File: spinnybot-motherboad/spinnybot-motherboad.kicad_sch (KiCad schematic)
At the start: 48 parts, among them J1 +12V, J11 CAP SWITCH, J12 LEDSTRIP3, J13 LEDSTRIP2, J14 LEDSTRIP3, J2 LEDSTRIP1, J3 LEDSTRIP1, J4 LEDSTRIP2, J5 GND, J6 MOTOR2, J7 MOTOR3, J8 MOTOR1, J9 CAP SWITCH, Q1 SISA96DN, Q2 SISA96DN, Q4 2N3904, Q5 2N3906, U1 LM1117-3.3, U2 XBP9B-DMWT-002, U3 SN74LVC1G74

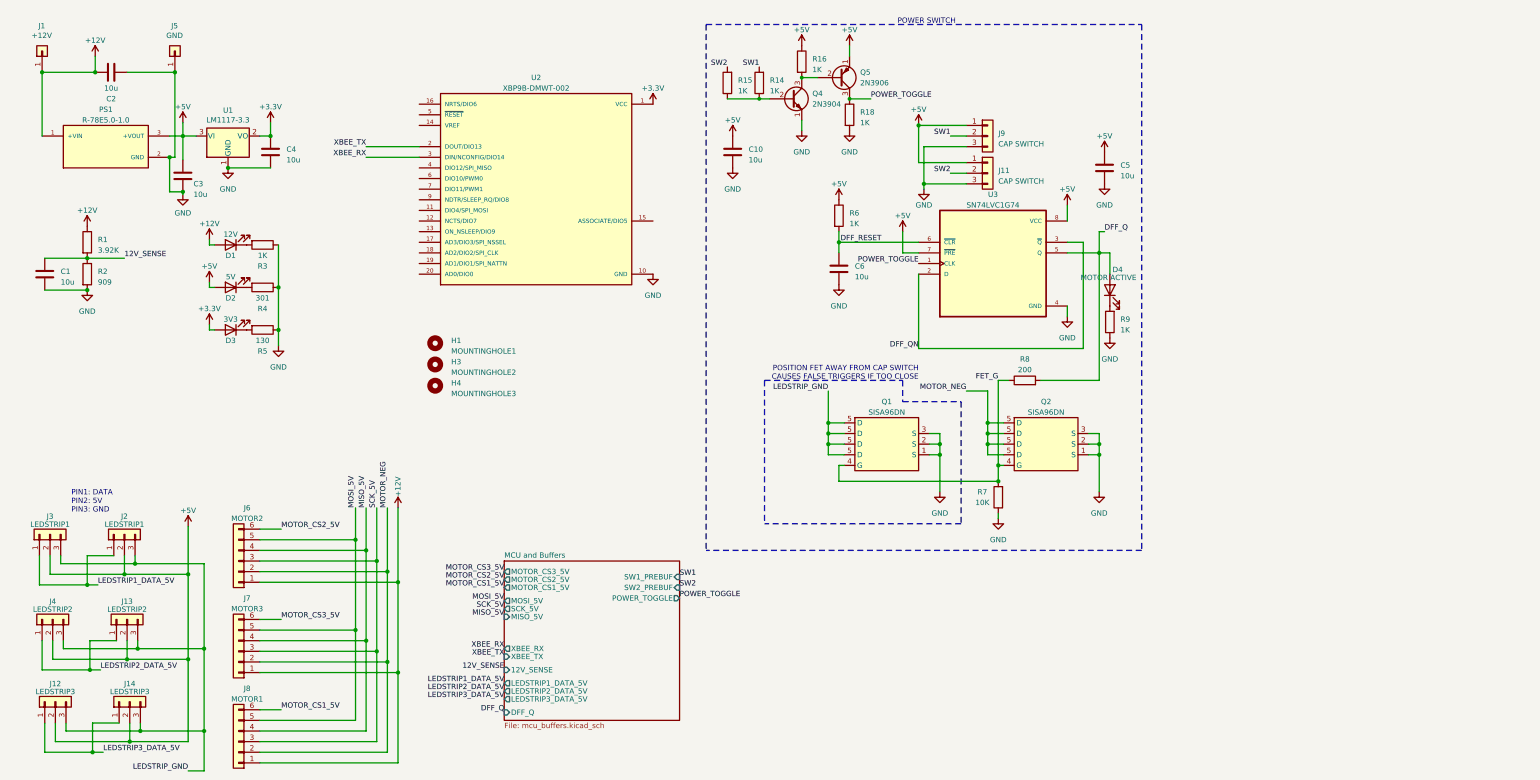
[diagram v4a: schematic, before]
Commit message: split schematic into multiple files and stole Erick's homework on redoing the power button
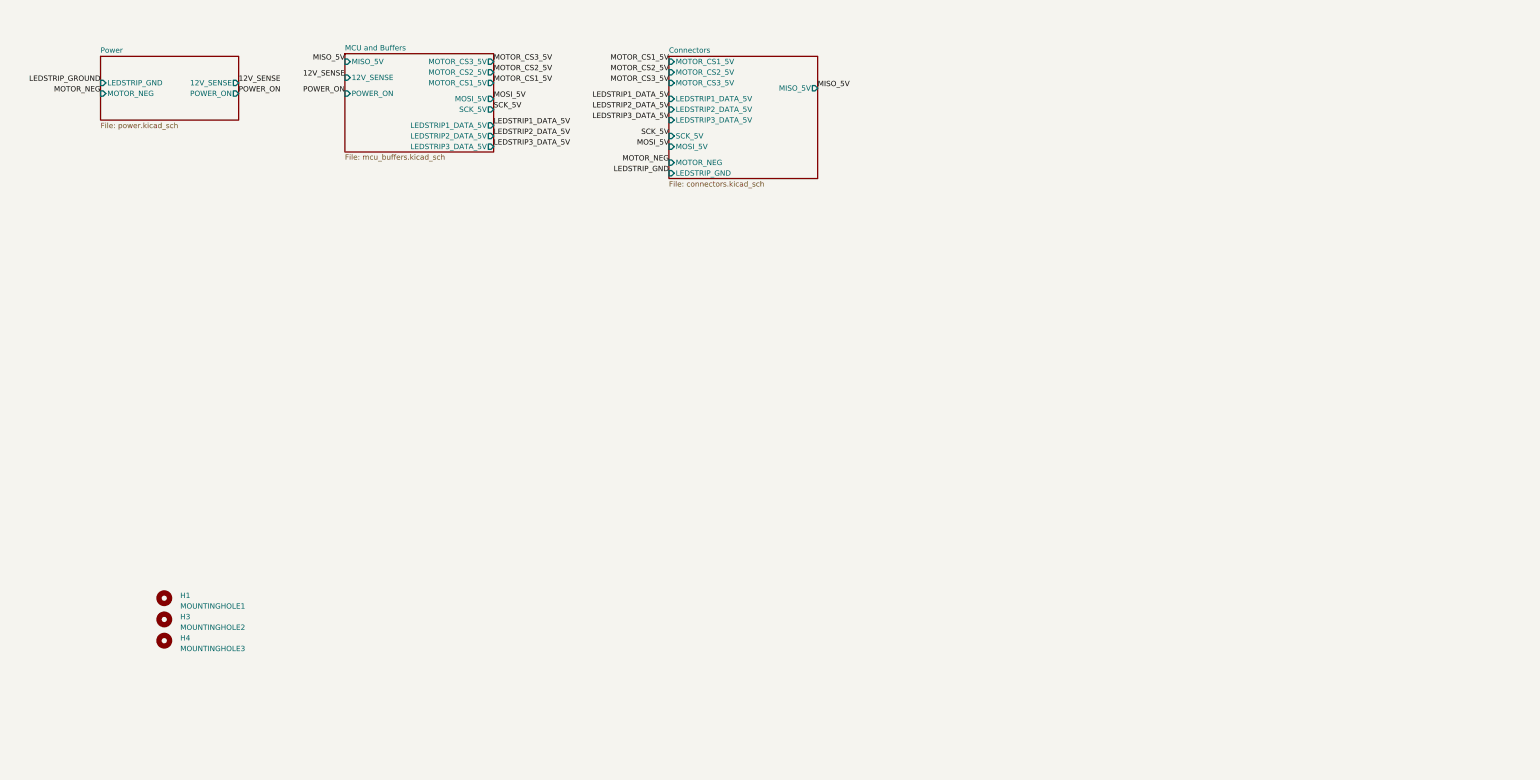
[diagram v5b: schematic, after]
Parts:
- removed C1, C10, C3, C4, C5, C6: 10u, Capacitor_SMD:C_1206_3216Metric_Pad1.33x1.80mm_HandSolder, symbol Device:C
- removed C2: 10u, Capacitor_SMD:C_0805_2012Metric_Pad1.18x1.45mm_HandSolder, symbol Device:C
- removed D1: 12V, LED_SMD:LED_0805_2012Metric_Pad1.15x1.40mm_HandSolder, symbol Device:LED
- removed D2: 5V, LED_SMD:LED_0805_2012Metric_Pad1.15x1.40mm_HandSolder, symbol Device:LED
- removed D3: 3V3, LED_SMD:LED_0805_2012Metric_Pad1.15x1.40mm_HandSolder, symbol Device:LED
- removed D4: MOTOR ACTIVE, LED_SMD:LED_0805_2012Metric_Pad1.15x1.40mm_HandSolder, symbol Device:LED
- removed J1: +12V, Connector_Wire:SolderWirePad_1x01_SMD_5x10mm, symbol Connector_Generic:Conn_01x01
- removed J11, J9: CAP SWITCH, B3B-PH-SM4:JST_B3B-PH-SM4-TB(LF)(SN), symbol Connector_Generic:Conn_01x03
- removed J12, J14: LEDSTRIP3, B3B-PH-SM4:JST_B3B-PH-SM4-TB(LF)(SN), symbol Connector_Generic:Conn_01x03
- removed J13, J4: LEDSTRIP2, B3B-PH-SM4:JST_B3B-PH-SM4-TB(LF)(SN), symbol Connector_Generic:Conn_01x03
- removed J2, J3: LEDSTRIP1, B3B-PH-SM4:JST_B3B-PH-SM4-TB(LF)(SN), symbol Connector_Generic:Conn_01x03
- removed J5: GND, custom:Stitched_SolderWirePad_1x01_SMD_5x10mm, symbol Connector_Generic:Conn_01x01
- removed J6: MOTOR2, S6B-XH-SM4-TB:S6B-XH-SM4-TBLFSN, symbol Connector_Generic:Conn_01x06
- removed J7: MOTOR3, S6B-XH-SM4-TB:S6B-XH-SM4-TBLFSN, symbol Connector_Generic:Conn_01x06
- removed J8: MOTOR1, S6B-XH-SM4-TB:S6B-XH-SM4-TBLFSN, symbol Connector_Generic:Conn_01x06
- removed PS1: R-78E5.0-1.0, R-78E5:CONV_R-78E5.0-1.0, symbol R-78E5.0-1.0:R-78E5.0-1.0
- removed Q1, Q2: SISA96DN, Package_SO:Vishay_PowerPAK_1212-8_Single, symbol spinnybot:SISA96DN
- removed Q4: 2N3904, Package_TO_SOT_THT:TO-92_Inline, symbol Transistor_BJT:2N3904
- removed Q5: 2N3906, Package_TO_SOT_THT:TO-92_Inline, symbol Transistor_BJT:2N3906
- removed R1: 3.92K, Resistor_SMD:R_0805_2012Metric_Pad1.20x1.40mm_HandSolder, symbol Device:R
- removed R14, R15, R16, R18, R3, R6, R9: 1K, Resistor_SMD:R_0805_2012Metric_Pad1.20x1.40mm_HandSolder, symbol Device:R
- removed R2: 909, Resistor_SMD:R_0805_2012Metric_Pad1.20x1.40mm_HandSolder, symbol Device:R
- removed R4: 301, Resistor_SMD:R_0805_2012Metric_Pad1.20x1.40mm_HandSolder, symbol Device:R
- removed R5: 130, Resistor_SMD:R_0805_2012Metric_Pad1.20x1.40mm_HandSolder, symbol Device:R
- removed R7: 10K, Resistor_SMD:R_0805_2012Metric_Pad1.20x1.40mm_HandSolder, symbol Device:R
- removed R8: 200, Resistor_SMD:R_0805_2012Metric_Pad1.20x1.40mm_HandSolder, symbol Device:R
- removed U1: LM1117-3.3, Package_TO_SOT_SMD:SOT-223-3_TabPin2, symbol Regulator_Linear:LM1117-3.3
- removed U2: XBP9B-DMWT-002, XBee_PRO900HP_S3B:DIP2200W51P200L3294H279Q20P, symbol XBee_PRO900HP_S3B:XBP9B-DMWT-002
- removed U3: SN74LVC1G74, SN74LVC1G74DCUR:SOP50P310X90-8N, symbol SN74LVC1G74DCUR:SN74LVC1G74DCUR
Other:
- added sheet Connectors (connectors.kicad_sch)
- added sheet Power (power.kicad_sch)
- sheet MCU and Buffers ports: added POWER_ON; removed DFF_Q, POWER_TOGGLE, SW1_PREBUF, SW2_PREBUF, XBEE_RX, XBEE_TX
- note removed: "PIN1: DATA PIN2: 5V PIN3: GND"
- note removed: "POSITION FET AWAY FROM CAP SWITCH CAUSES FALSE TRIGGERS IF TOO CLOSE"
- note removed: "POWER SWITCH"
- moved on the sheet: H1, H3, H4
